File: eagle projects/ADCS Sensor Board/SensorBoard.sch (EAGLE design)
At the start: 102 parts, among them J1 HDR_10_EZFET_DEBUGGER, J2 MTI-1_8428-11B1-RK-TP, J3 HDR_2X5_GRPB052VWQS-RC, Q1 PMV16XN, Q2 IRLML6246TRPBF, Q3 IRLML2246TRPBF, U1 MSP430F5529IPN, U2 LMV321, U3 ADS7841E_2K5, U4 LMV321, U5 LMV321, Y1 32.768kHz, Y2 CSTCR4M00G15L99

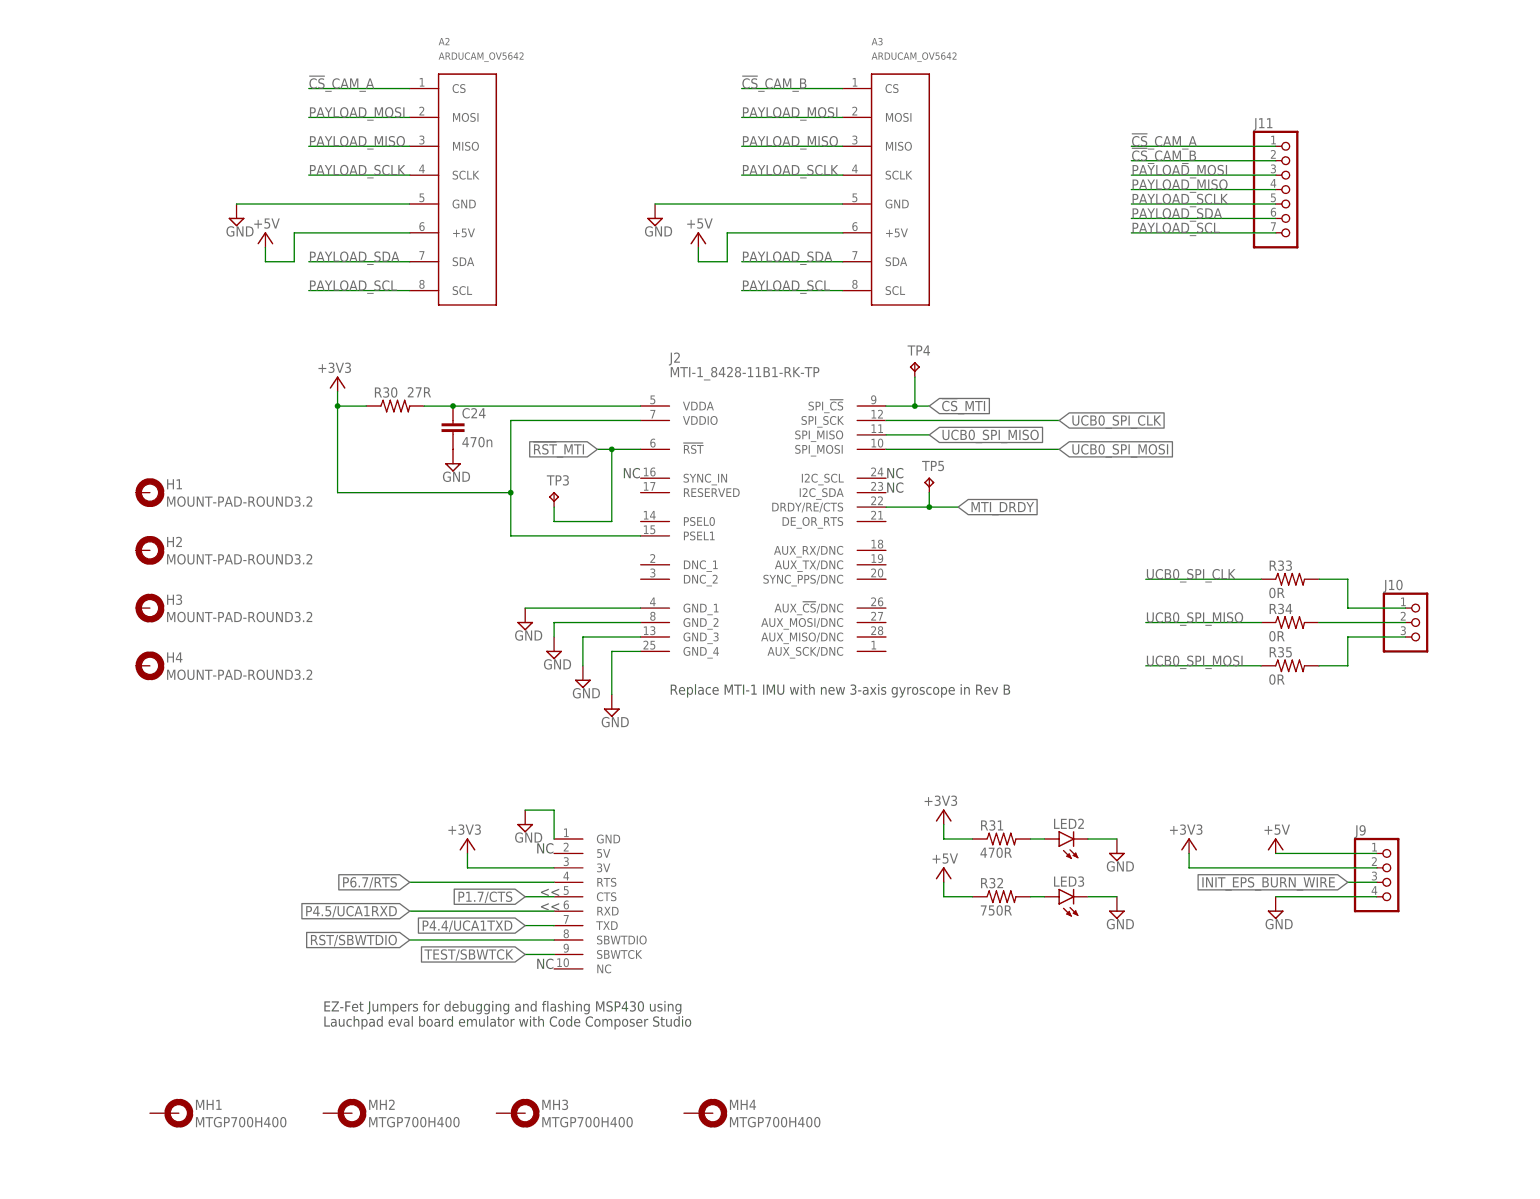
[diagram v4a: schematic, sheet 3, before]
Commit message: Added BNO055 IMU to sensor board schematic
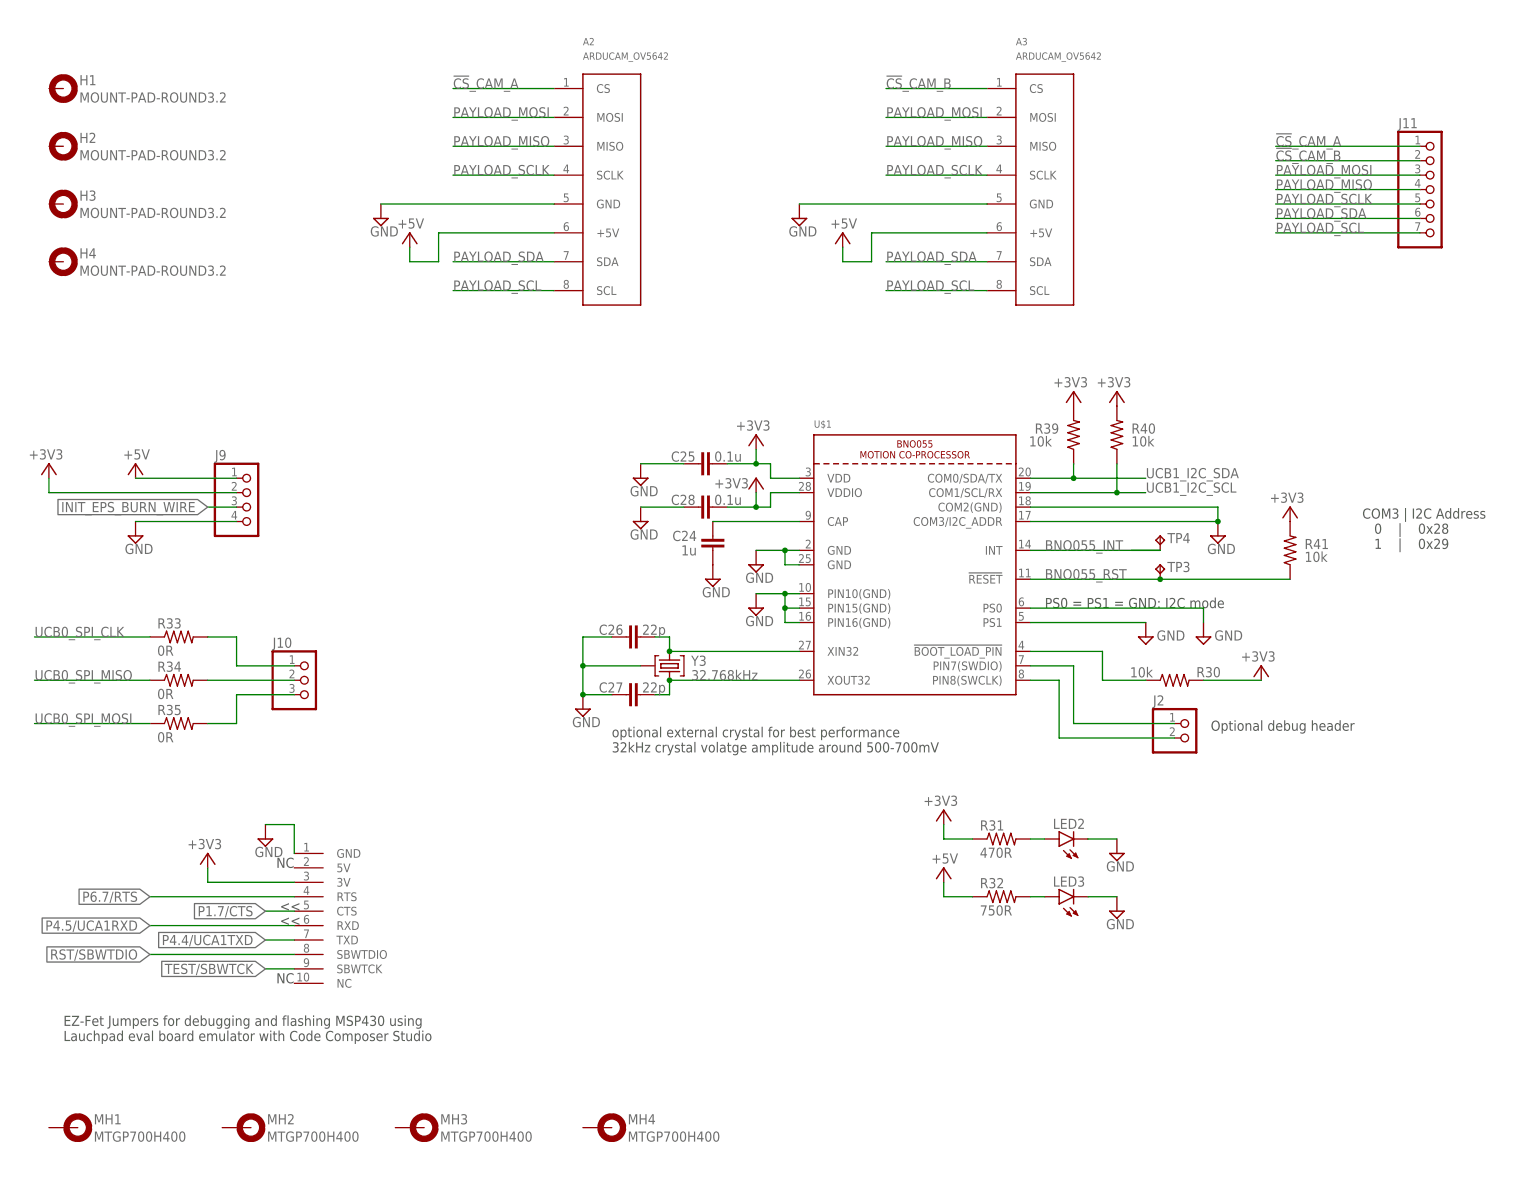
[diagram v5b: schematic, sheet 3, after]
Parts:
- removed TP5: TESTPOINT, my_library:TESTPOINT
- added C25, C28: 0.1u, rcl:C-EUC0402
- added C26, C27: 22p, rcl:C-EUC0402
- added R39, R40, R41: 10k, rcl:R-US_R0402
- added U$1: (no value), my_library:BNO055
- added Y3: 32.768kHz, my_library:MS3V-T1R
- C24: value 470n -> 1u; device rcl:C-EUC0805 -> rcl:C-EUC0402
- J2: value MTI-1_8428-11B1-RK-TP -> (none); device my_library:MTI-1_8428-11B1-RK-TP -> my_library:HDR_1X2_
- R30: value 27R -> 10k; device rcl:R-US_R0805 -> rcl:R-US_R0402
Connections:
- new net BNO055_INT: TP4.TP, U$1.INT
- new net BNO055_RST: R41.1, TP3.TP, U$1.!RESET
- new net N$13: C24.2, U$1.CAP
- new net N$14: C26.2, U$1.XIN32, Y3.2
- new net N$15: C27.2, U$1.XOUT32, Y3.1
- new net N$16: J2.1, U$1.PIN7(SWDIO)
- new net N$17: J2.2, U$1.PIN8(SWCLK)
- net !CS!_MTI: no longer J2.SPI_!CS, TP4.TP
- net !RST!_MTI: no longer J2.!RST, TP3.TP
- net +3V3: now also C25.2, C28.2, R30.2, R39.2, R40.2, R41.2, U$1.VDD, U$1.VDDIO; no longer J2.PSEL1, J2.VDDIO, R30.1
- net GND: now also C25.1, C26.1, C27.1, C28.1, U$1.COM2(GND), U$1.COM3/I2C_ADDR, U$1.GND@1, U$1.GND@2, U$1.PIN10(GND), U$1.PIN15(GND), U$1.PIN16(GND), U$1.PS0, U$1.PS1, Y3.GND; no longer J2.GND_1, J2.GND_2, J2.GND_3, J2.GND_4
- net MTI_DRDY: no longer J2.DRDY/RE/CTS, TP5.TP
- net N$7: now also R30.1, U$1.!BOOT_LOAD_PIN; no longer C24.2, J2.VDDA, R30.2
- net UCB0_SPI_CLK: no longer J2.SPI_SCK
- net UCB0_SPI_MISO: no longer J2.SPI_MISO
- net UCB0_SPI_MOSI: no longer J2.SPI_MOSI
- net UCB1_I2C_SCL: now also R40.1, U$1.COM1/SCL/RX
- net UCB1_I2C_SDA: now also R39.1, U$1.COM0/SDA/TX
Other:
- note added: "COM3 | I2C Address 0 | 0x28 1 | 0x29"
- note added: "Optional debug header"
- note added: "PS0 = PS1 = GND: I2C mode"
- note added: "optional external crystal for best performance 32kHz crystal volatge amplitude around 500-700mV"
- note removed: "Replace MTI-1 IMU with new 3-axis gyroscope in Rev B"
- moved on the sheet: A2, A3, C24, H1, H2, H3, H4, J10, J11, J9, MH1, MH2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

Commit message: Schematic Updates
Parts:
- removed A1: HMC1053PA0242, my_library:HMC1053PA0242
- removed J5: (no value), my_library:PINHD-2X8
- removed J7, J8, J9: (no value), my_library:PINHD-1X4
- removed U$1: (no value), my_library:BNO055
- added C29: 0.1u, rcl:C-EUC0603
- added JP1: (no value), pinhead:PINHD-1X3
- added JP2: (no value), pinhead:PINHD-2X5
- added JP3: (no value), pinhead:PINHD-2X3
- added JP4: (no value), my_library:PINHD-1X6
- added R37: 10k, rcl:R-US_R0805
- added TP5: TESTPOINT, my_library:TESTPOINT
- added U6: (no value), my_library:BNO055
- added U7: HMC1053, my_library:HMC1053
- C10: value 0.1u -> 1u
- C18: value 1n -> 0.1u
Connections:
- removed net !COUNT_EN: J5.5, U1.P7.1/CB9/A13
- removed net !CS!_SPEED_X: J5.8, U1.P6.6/CB6/A6
- removed net !CS!_SPEED_Y: J5.10, U1.P6.5/CB5/A5
- removed net !CS!_SPEED_Z: J5.12, U1.P7.0/CB8/A12
- removed net !LOAD_SPEED: J5.9, U1.P7.3/CB11/A15
- removed net !SPEED_CLR: J5.7, U1.P7.2/CB10/A14
- new net N$18: JP2.8
- new net N$19: JP2.10
- new net N$29: TP5.TP, U3.CH0
- new net N$31: C29.1, R37.2, U3.!SHDN
- net !CS!_CURRENT_SENSE_1: now also JP3.1; no longer J5.11
- net !CS!_CURRENT_SENSE_2: now also JP3.3; no longer J5.13
- net !CS!_SUN_X+: now also JP2.2; no longer J5.16
- net !CS!_SUN_X-: now also JP2.7; no longer J5.14
- net !CS!_SUN_Y+: now also JP2.4; no longer J5.3
- net !CS!_SUN_Y-: now also JP2.9; no longer J5.1
- net !CS!_SUN_Z+: now also JP4.5; no longer J8.2
- net !CS!_SUN_Z-: now also JP2.6; no longer J7.2
- net +3V3: now also JP1.2, JP4.1, R37.1, U6.VDD, U6.VDDIO, U7.VB; no longer A1.VB, J9.2, U$1.VDD, U$1.VDDIO, U3.!SHDN
- net +5V: now also JP1.1; no longer J9.1
- net ACT_BRD_3V_PRESENT: now also JP3.5; no longer J5.15
- net BNO055_INT: now also U6.INT; no longer U$1.INT
- net BNO055_RST: now also U6.!RESET; no longer U$1.!RESET
- net GND: now also C29.2, JP1.3, JP4.6, U6.COM2(GND), U6.COM3/I2C_ADDR, U6.GND@1, U6.GND@2, U6.PIN10(GND), U6.PIN15(GND), U6.PIN16(GND), U6.PS0, U6.PS1, U7.GND(A), U7.GND(B), U7.GND(C), U7.S/R-(A,B,C); no longer A1.GND(A), A1.GND(B), A1.GND(C), A1.S/R-(A,B,C), J9.4, U$1.COM2(GND), U$1.COM3/I2C_ADDR, U$1.GND@1, U$1.GND@2, U$1.PIN10(GND), U$1.PIN15(GND), U$1.PIN16(GND), U$1.PS0, U$1.PS1
- net INIT_EPS_BURN_WIRE: no longer J9.3
- net N$13: now also U6.CAP; no longer U$1.CAP
- net N$14: now also U6.XIN32, Y3.1; no longer U$1.XIN32, Y3.2
- net N$15: now also U6.XOUT32, Y3.2; no longer U$1.XOUT32, Y3.1
- net N$16: now also U6.PIN7(SWDIO); no longer U$1.PIN7(SWDIO)
- net N$17: now also U6.PIN8(SWCLK); no longer U$1.PIN8(SWCLK)
- net N$36: now also U7.OFF+(A,B,C), U7.OFF-(A,B), U7.OFF-(C); no longer A1.OFF+(A,B,C), A1.OFF-(A,B), A1.OFF-(C)
- net N$37: now also U7.S/R+(A,B), U7.S/R+(C); no longer A1.S/R+(A,B), A1.S/R+(C)
- net N$7: now also U6.!BOOT_LOAD_PIN; no longer U$1.!BOOT_LOAD_PIN
- net OUT_A_N: now also U7.OUT-(A); no longer A1.OUT-(A)
- net OUT_A_P: now also U7.OUT+(A); no longer A1.OUT+(A)
- net OUT_B_N: now also U7.OUT-(B); no longer A1.OUT-(B)
- net OUT_B_P: now also U7.OUT+(B); no longer A1.OUT+(B)
- net OUT_C_N: now also U7.OUT-(C); no longer A1.OUT-(C)
- net OUT_C_P: now also U7.OUT+(C); no longer A1.OUT+(C)
- net UCB0_SPI_CLK: now also JP2.5, JP3.2, JP4.4; no longer J5.2, J7.1, J8.1
- net UCB0_SPI_MISO: now also JP2.1, JP3.4, JP4.2; no longer J5.4, J7.4, J8.4
- net UCB0_SPI_MOSI: now also JP2.3, JP3.6, JP4.3; no longer J5.6, J7.3, J8.3
- net UCB1_I2C_SCL: now also U6.COM1/SCL/RX; no longer U$1.COM1/SCL/RX
- net UCB1_I2C_SDA: now also U6.COM0/SDA/TX; no longer U$1.COM0/SDA/TX
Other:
- note added: "*Add 3.3V overvoltage protection on pins 7, 9, 2, and 4 on next rev"
- note added: "Mounting holes for connected Z- SUN SENSE BOARD"
- note added: "Optional UART bus debug header (standard pitch)"

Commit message: Added some notes
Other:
- note added: "BNO055 INT BNO055 RST"
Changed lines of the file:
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@@
 <text x="175.26" y="73.66" size="1.778" layer="91">was !CS!_SUN_Y+</text>
 <text x="175.26" y="71.12" size="1.778" layer="91">was !CS!_SUN_Z+</text>
+<text x="27.94" y="45.72" size="1.778" layer="91">BNO055 INT
+BNO055 RST</text>
 </plain>
 <instances>
@@
 <sheet>
 <plain>
-<attribute name="NAME" x="39.37" y="191.135" size="1.778" layer="95"/>
-<attribute name="VALUE" x="39.37" y="175.26" size="1.778" layer="96"/>
 <text x="91.44" y="137.16" size="1.778" layer="97" grouprefs="ACTUATOR_BOARD_CONNECTORS">PWM</text>
 <text x="91.44" y="134.62" size="1.778" layer="97" grouprefs="ACTUATOR_BOARD_CONNECTORS">PWM</text>
@@
 <text x="17.78" y="134.62" size="1.778" layer="97" grouprefs="ACTUATOR_BOARD_CONNECTORS">PWM</text>
 <text x="17.78" y="132.08" size="1.778" layer="97" grouprefs="ACTUATOR_BOARD_CONNECTORS">PWM</text>
-<attribute name="NAME" x="54.61" y="140.335" size="1.778" layer="95"/>
-<attribute name="VALUE" x="54.61" y="114.3" size="1.778" layer="96"/>
 <text x="66.04" y="101.6" size="1.778" layer="97">OBC CONNECTOR</text>
 <text x="139.7" y="104.14" size="1.778" layer="97">&lt;&lt;</text>
@@
 <text x="228.6" y="109.22" size="1.778" layer="97" grouprefs="EZFET_DEBUGGER_HEADER">&lt;&lt;</text>
 <text x="228.6" y="106.68" size="1.778" layer="97" grouprefs="EZFET_DEBUGGER_HEADER">&gt;&gt;</text>
-<attribute name="VALUE" x="205.74" y="195.58" size="1.778" layer="96" rot="R180"/>
-<attribute name="VALUE" x="198.12" y="193.04" size="1.778" layer="96" rot="R180"/>
-<attribute name="VALUE" x="201.295" y="174.625" size="1.778" layer="96"/>
-<attribute name="VALUE" x="224.155" y="121.285" size="1.778" layer="96"/>
-<attribute name="VALUE" x="218.44" y="124.46" size="1.778" layer="96" rot="R180"/>
-<attribute name="NAME" x="227.33" y="158.115" size="1.778" layer="95"/>
-<attribute name="VALUE" x="227.33" y="144.78" size="1.778" layer="96"/>
-<attribute name="NAME" x="207.01" y="146.2786" size="1.778" layer="95"/>
-<attribute name="VALUE" x="207.01" y="141.478" size="1.778" layer="96"/>
-<attribute name="NAME" x="207.01" y="153.8986" size="1.778" layer="95"/>
-<attribute name="VALUE" x="207.01" y="149.098" size="1.778" layer="96"/>
-<attribute name="NAME" x="207.01" y="161.5186" size="1.778" layer="95"/>
-<attribute name="VALUE" x="207.01" y="156.718" size="1.778" layer="96"/>
-<attribute name="NAME" x="73.66" y="-12.7" size="1.27" layer="95"/>
-<attribute name="VALUE" x="73.66" y="-15.24" size="1.27" layer="96"/>
-<attribute name="NAME" x="149.86" y="-12.7" size="1.27" layer="95"/>
-<attribute name="VALUE" x="149.86" y="-15.24" size="1.27" layer="96"/>
-<attribute name="VALUE" x="36.195" y="-46.355" size="1.778" layer="96"/>
-<attribute name="VALUE" x="109.855" y="-46.355" size="1.778" layer="96"/>
-<attribute name="VALUE" x="45.72" y="-43.18" size="1.778" layer="96" rot="R180"/>
-<attribute name="VALUE" x="121.92" y="-43.18" size="1.778" layer="96" rot="R180"/>
-<attribute name="NAME" x="217.17" y="-27.305" size="1.778" layer="95"/>
-<attribute name="VALUE" x="217.17" y="-48.26" size="1.778" layer="96"/>
 <text x="119.38" y="187.96" size="1.778" layer="97">Optional UART bus debug header (standard pitch)</text>
 <text x="68.58" y="180.34" size="1.778" layer="97">NC</text>
